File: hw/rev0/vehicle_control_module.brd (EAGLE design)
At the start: 160 x 100 mm, 494 parts, among them IC1 SJA1105TELY, IC10 TJA1100HNZ, IC11 KSZ8061MNXI-TR, IC12 TJA1100HNZ, IC13 TLE9250XSJXUMA1, IC17 LP5907QMFX-3.3Q1, IC18 TLE9250XSJXUMA1, IC2 ATSAMV71Q21B-AABT, IC3 TJA1100HNZ, IC4 FT2232HL, IC5 TRS3232EQPWRQ1, IC6 SST26VF032BT-104I_SM, IC7 DS3231SN#, IC8 74HC7541D-Q100J, IC9 TPS62242DRVR, J10 5-2337992-3, J11 2301843-1, J12 1017505, J13 2301843-1, J15 693022010811, J2 2305018-2, J27 2041119-2, J3 1017505, J4 1017505, J5 1017505, J6 1017505, J7 1017505, J8 1017505, J9 1017505, U1 122-2920-GR, U2 LM63625, U3 TPS62007-Q1_DGS_10, Y1 NX3225SA-25MHZ-EXS00A-CS11338, Y3 ABM8AIG-12.000MHZ-1Z-T

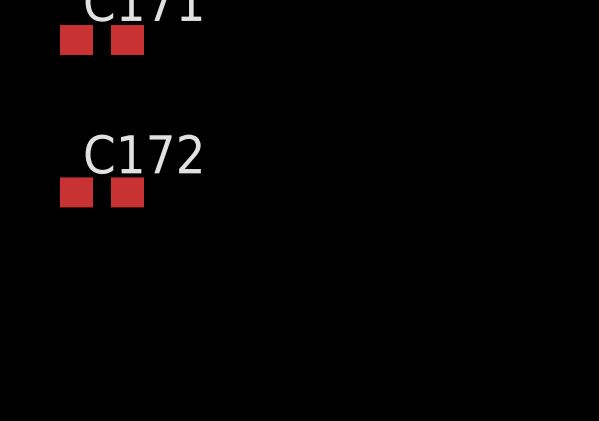
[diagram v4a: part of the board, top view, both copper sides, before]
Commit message: Add schematic for test tool based on the full vehicle control module design
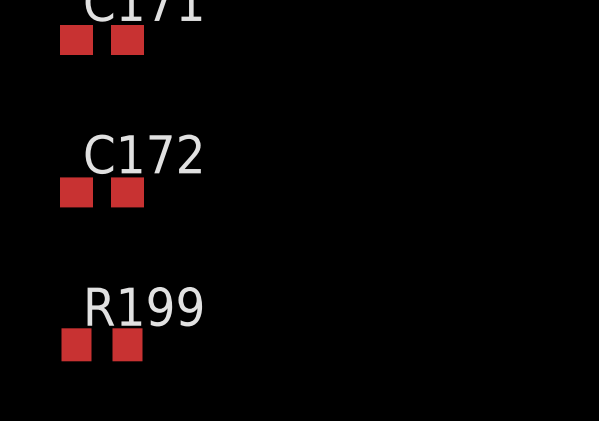
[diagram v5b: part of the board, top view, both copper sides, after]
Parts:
- added R199: 10k, rcl:R0603
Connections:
- net GND: now also R199.2
- net PHY_RST: now also IC2.120, R199.1
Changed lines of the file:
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@@
 <attribute name="VALUE" x="-291.465" y="858.52" size="1.27" layer="27" rot="R90"/>
+</element>
+<element name="R199" library="rcl" library_urn="urn:adsk.eagle:library:334" package="R0603" package3d_urn="urn:adsk.eagle:package:23555/3" value="10k" x="-294.64" y="-1485.9" smashed="yes">
+<attribute name="NAME" x="-295.275" y="-1485.265" size="1.27" layer="25"/>
+<attribute name="POPULARITY" value="77" x="-294.64" y="-1485.9" size="1.778" layer="27" display="off"/>
+<attribute name="SPICEPREFIX" value="R" x="-294.64" y="-1485.9" size="1.778" layer="27" display="off"/>
+<attribute name="VALUE" x="-295.275" y="-1487.805" size="1.27" layer="27"/>
 </element>
 </elements>
@@
 <contactref element="LED15" pad="C"/>
 <contactref element="LED16" pad="C"/>
+<contactref element="R199" pad="2"/>
 <wire x1="-293.79" y1="-1475.74" x2="-293.79" y2="-1480.82" width="0" layer="19" extent="1-1"/>
 <wire x1="-293.79" y1="-1470.66" x2="-293.79" y2="-1475.74" width="0" layer="19" extent="1-1"/>
@@
 <wire x1="-293.79" y1="-1404.62" x2="-293.79" y2="-1409.7" width="0" layer="19" extent="1-1"/>
 <wire x1="-293.79" y1="-1399.54" x2="-293.79" y2="-1404.62" width="0" layer="19" extent="1-1"/>
+<wire x1="-293.79" y1="-1485.9" x2="-293.79" y2="-1480.82" width="0" layer="19" extent="1-1"/>
 <wire x1="-295.49" y1="-1394.46" x2="-293.79" y2="-1399.54" width="0" layer="19" extent="1-1"/>
 <wire x1="-293.015" y1="-1384.935" x2="-295.49" y2="-1394.46" width="0" layer="19" extent="1-1"/>
@@
 <contactref element="IC10" pad="3"/>
 <contactref element="IC12" pad="3"/>
+<contactref element="IC2" pad="120"/>
+<contactref element="R199" pad="1"/>
 <wire x1="-140.01" y1="-730.52" x2="-140.01" y2="-778.78" width="0" layer="19" extent="1-1"/>
-<wire x1="37.79" y1="36.56" x2="-140.01" y2="-730.52" width="0" layer="19" extent="1-1"/>
+<wire x1="-295.49" y1="-1485.9" x2="-140.01" y2="-778.78" width="0" layer="19" extent="1-1"/>
+<wire x1="15.95" y1="-1.962" x2="-140.01" y2="-730.52" width="0" layer="19" extent="1-1"/>
+<wire x1="37.79" y1="36.56" x2="15.95" y2="-1.962" width="0" layer="19" extent="1-1"/>
 </signal>
 <signal name="N$13">

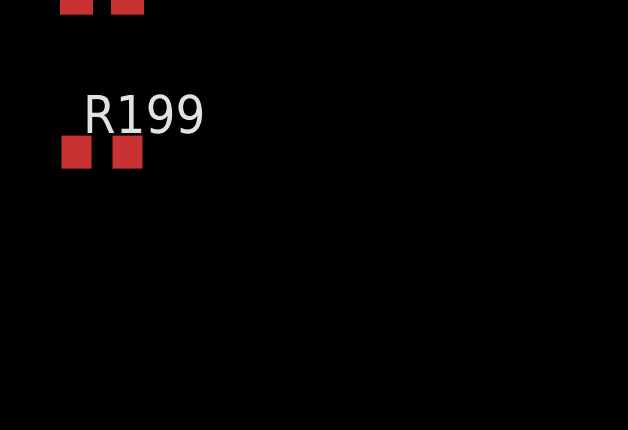
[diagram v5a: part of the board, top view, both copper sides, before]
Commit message: Add missing oscillator, start to layout testtool board
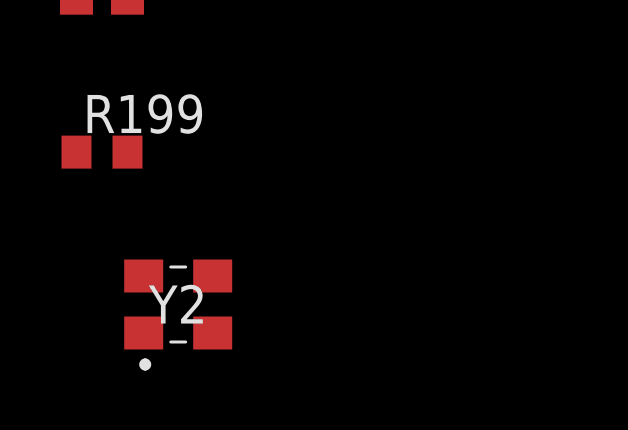
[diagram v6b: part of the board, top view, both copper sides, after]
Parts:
- added Y2: ABM8AIG-12.000MHZ-12-D2Z-T, samacsys:ABM8AIG12000MHZ12D2ZT
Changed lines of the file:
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@@
 <attribute name="VALUE" x="-295.275" y="-1487.805" size="1.27" layer="27"/>
+</element>
+<element name="Y2" library="samacsys" package="ABM8AIG12000MHZ12D2ZT" value="ABM8AIG-12.000MHZ-12-D2Z-T" x="-292.1" y="-1490.98" smashed="yes">
+<attribute name="DESCRIPTION" value="ABRACON - ABM8AIG-12.000MHZ-12-D2Z-T - CRYSTAL, AECQ200, 12MHZ, 12PF, 3.2X2.5MM" x="-292.1" y="-1490.98" size="1.778" layer="27" display="off"/>
+<attribute name="HEIGHT" value="0.8mm" x="-292.1" y="-1490.98" size="1.778" layer="27" display="off"/>
+<attribute name="MANUFACTURER_NAME" value="ABRACON" x="-292.1" y="-1490.98" size="1.778" layer="27" display="off"/>
+<attribute name="MANUFACTURER_PART_NUMBER" value="ABM8AIG-12.000MHz-12-D2Z-T" x="-292.1" y="-1490.98" size="1.778" layer="27" display="off"/>
+<attribute name="MOUSER_PART_NUMBER" value="815-ABM8AIG1212D2ZT" x="-292.1" y="-1490.98" size="1.778" layer="27" display="off"/>
+<attribute name="MOUSER_PRICE-STOCK" value="https://www.mouser.com/Search/Refine.aspx?Keyword=815-ABM8AIG1212D2ZT" x="-292.1" y="-1490.98" size="1.778" layer="27" display="off"/>
+<attribute name="NAME" x="-292.1" y="-1490.98" size="1.27" layer="25" align="center"/>
+<attribute name="RS_PART_NUMBER" value="" x="-292.1" y="-1490.98" size="1.778" layer="27" display="off"/>
+<attribute name="RS_PRICE-STOCK" value="" x="-292.1" y="-1490.98" size="1.778" layer="27" display="off"/>
+<attribute name="VALUE" x="-292.1" y="-1490.98" size="1.27" layer="27" align="center"/>
 </element>
 </elements>
